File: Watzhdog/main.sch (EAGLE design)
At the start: 45 parts, among them IC1 C8051F381-GM, IC3 N25Q512A, IC6 MPU-9250, U1 MCP73831, U2 TPS61201

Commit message: Routed some airwires
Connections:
- removed net GND: C1.2, C12.2, C3.2, C4.2, C5.2, JP1.-, JP9.GND, R1.2, R4.2, R5.1, U1.VSS, U2.GND, U2.PAD@1, U2.PAD@2, U2.PAD@3, U2.PAD@4, U2.PAD@5, U2.PGND, U2.PS
- net DGND: now also C1.2, C12.2, C3.2, C4.2, C5.2, JP1.-, JP9.GND, R1.2, R4.2, R5.1, U1.VSS, U2.GND, U2.PAD@1, U2.PAD@2, U2.PAD@3, U2.PAD@4, U2.PAD@5, U2.PGND, U2.PS

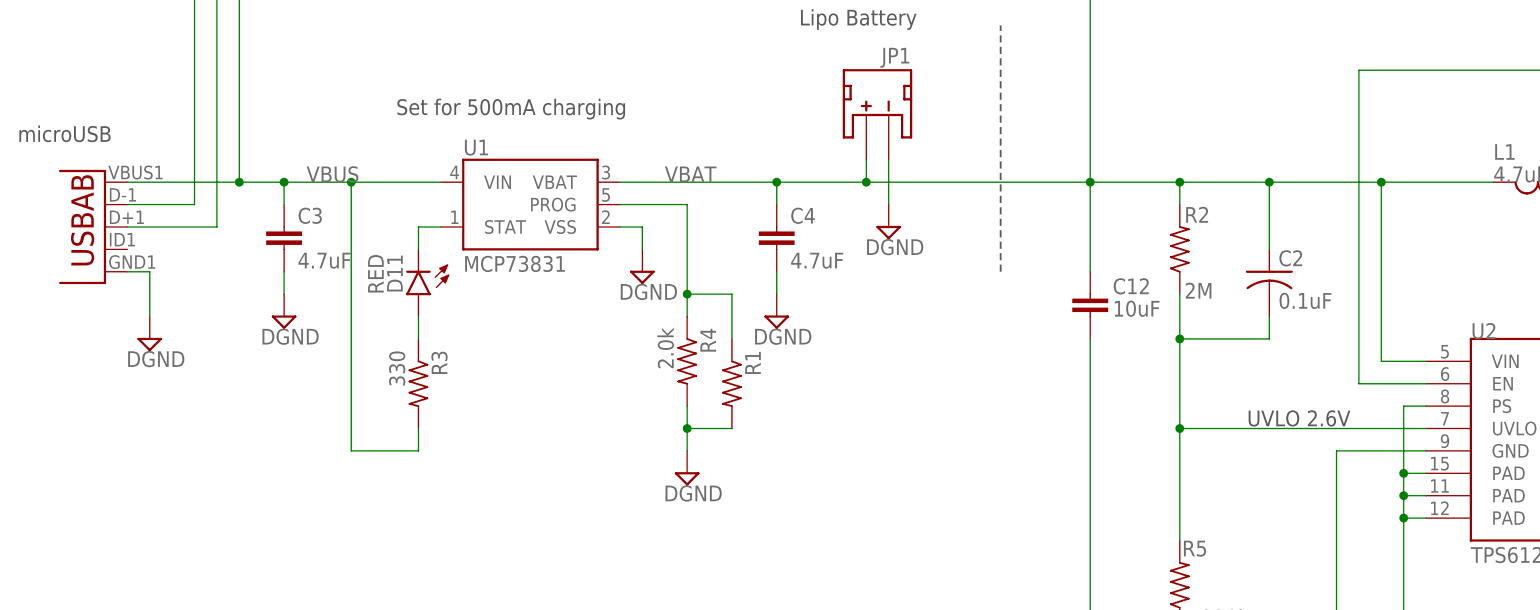
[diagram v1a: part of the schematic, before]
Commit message: Delete unnecessary resistances
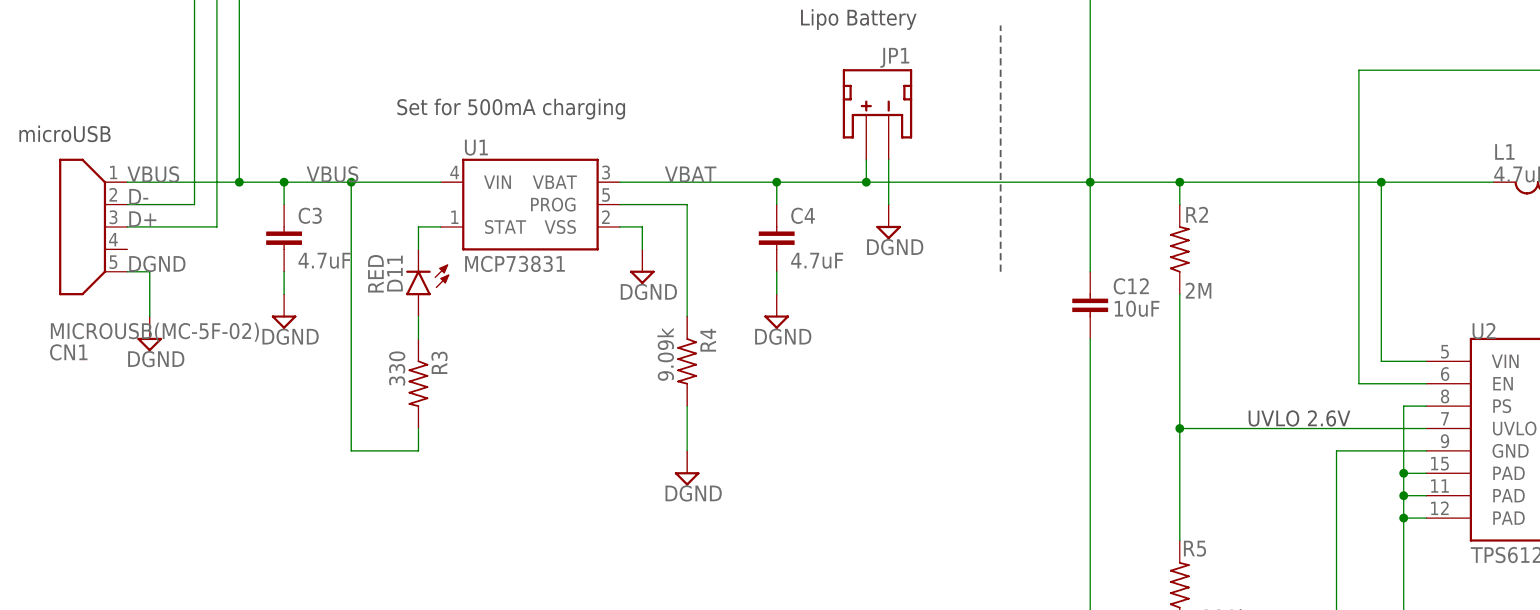
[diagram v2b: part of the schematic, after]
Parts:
- removed C2: 0.1uF, rcl:C-USC0402K
- removed JP9: Micro USB, SparkFun-Connectors:USB-ABCONN-11794
- removed R1: (no value), rcl:R-US_R0402
- added CN1: MICROUSB(MC-5F-02), Connector:MICROUSB(MC-5F-02)
- R4: value 2.0k -> 9.09k
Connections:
- net D+: now also CN1.P$3; no longer JP9.D+
- net D-: now also CN1.P$2; no longer JP9.D-
- net DGND: now also CN1.P$5; no longer JP9.GND, R1.2
- net PROG: no longer R1.1
- net UVLO: no longer C2.2
- net VBAT: no longer C2.1
- net VBUS: now also CN1.P$1; no longer JP9.VBUS
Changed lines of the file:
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@@
 <part name="GND18" library="supply2" library_urn="urn:adsk.eagle:library:372" deviceset="DGND" device=""/>
 <part name="U1" library="SparkFun-PowerIC" deviceset="MCP73831" device=""/>
-<part name="R4" library="rcl" library_urn="urn:adsk.eagle:library:334" deviceset="R-US_" device="R0402" package3d_urn="urn:adsk.eagle:package:23547/2" value="2.0k"/>
+<part name="R4" library="rcl" library_urn="urn:adsk.eagle:library:334" deviceset="R-US_" device="R0402" package3d_urn="urn:adsk.eagle:package:23547/2" value="9.09k"/>
 <part name="GND19" library="supply2" library_urn="urn:adsk.eagle:library:372" deviceset="DGND" device=""/>
 <part name="C3" library="SparkFun-Capacitors" deviceset="4.7UF-6.3V-10%(0603)" device="0603" value="4.7uF"/>
 <part name="C4" library="SparkFun-Capacitors" deviceset="4.7UF-6.3V-10%(0603)" device="0603" value="4.7uF"/>
-<part name="JP9" library="SparkFun-Connectors" deviceset="USB-AB" device="CONN-11794" value="Micro USB"/>
 <part name="JP1" library="SparkFun-Connectors" deviceset="JST_2MM_MALE" device="" value="JST"/>
 <part name="C1" library="CH_passive" deviceset="CAP" device="0805" value="22uF"/>
 <part name="U2" library="SparkFun" deviceset="TPS61200" device="" value="TPS61201"/>
-<part name="C2" library="rcl" library_urn="urn:adsk.eagle:library:334" deviceset="C-US" device="C0402K" package3d_urn="urn:adsk.eagle:package:23679/2" value="0.1uF"/>
 <part name="C5" library="rcl" library_urn="urn:adsk.eagle:library:334" deviceset="C-US" device="C0402K" package3d_urn="urn:adsk.eagle:package:23679/2" value="0.1uF"/>
 <part name="R2" library="rcl" library_urn="urn:adsk.eagle:library:334" deviceset="R-US_" device="R0402" package3d_urn="urn:adsk.eagle:package:23547/2" value="2M"/>
@@
 <part name="SUPPLY3" library="supply2" deviceset="DGND" device=""/>
 <part name="SUPPLY5" library="supply2" deviceset="DGND" device=""/>
-<part name="R1" library="rcl" library_urn="urn:adsk.eagle:library:334" deviceset="R-US_" device="R0402" package3d_urn="urn:adsk.eagle:package:23547/2"/>
 <part name="MN" library="testpad" deviceset="PTR1" device="TP10R"/>
 <part name="MP" library="testpad" deviceset="PTR1" device="TP10R"/>
@@
 <part name="JP3" library="pinhead" library_urn="urn:adsk.eagle:library:325" deviceset="PINHD-1X3" device="" package3d_urn="urn:adsk.eagle:package:22458/2"/>
 <part name="C12" library="CH_passive" deviceset="CAP" device="1206" value="10uF"/>
+<part name="CN1" library="Connector" deviceset="MICROUSB(MC-5F-02)" device=""/>
 </parts>
 <sheets>
@@
 <instance part="C3" gate="G$1" x="25.4" y="15.24"/>
 <instance part="C4" gate="G$1" x="81.28" y="15.24"/>
-<instance part="JP9" gate="G$1" x="2.54" y="17.78" smashed="yes" rot="R180"/>
 <instance part="JP1" gate="G$1" x="93.98" y="30.48" rot="MR0"/>
 <instance part="C1" gate="G$1" x="215.9" y="-7.62" smashed="yes">
@@
 </instance>
 <instance part="U2" gate="G$1" x="172.72" y="-5.08"/>
-<instance part="C2" gate="G$1" x="137.16" y="12.7"/>
 <instance part="C5" gate="G$1" x="198.12" y="-22.86"/>
 <instance part="R2" gate="G$1" x="127" y="15.24" smashed="yes" rot="R90">
@@
 <instance part="SUPPLY3" gate="G$1" x="375.92" y="-86.36"/>
 <instance part="SUPPLY5" gate="G$1" x="353.06" y="-86.36"/>
-<instance part="R1" gate="G$1" x="76.2" y="0" rot="R270"/>
 <instance part="MN" gate="G$1" x="350.52" y="-63.5" rot="R270"/>
 <instance part="MP" gate="G$1" x="350.52" y="-55.88" rot="R270"/>
@@
 <attribute name="VALUE" x="119.38" y="7.62" size="1.778" layer="96"/>
 </instance>
+<instance part="CN1" gate="G$1" x="0" y="17.78"/>
 </instances>
 <busses>
@@
 <segment>
 <wire x1="127" y1="20.32" x2="127" y2="22.86" width="0.1524" layer="91"/>
-<wire x1="127" y1="22.86" x2="137.16" y2="22.86" width="0.1524" layer="91"/>
-<wire x1="137.16" y1="22.86" x2="149.86" y2="22.86" width="0.1524" layer="91"/>
+<wire x1="127" y1="22.86" x2="149.86" y2="22.86" width="0.1524" layer="91"/>
 <wire x1="116.84" y1="12.7" x2="116.84" y2="22.86" width="0.1524" layer="91"/>
 <wire x1="116.84" y1="22.86" x2="127" y2="22.86" width="0.1524" layer="91"/>
 <wire x1="162.56" y1="22.86" x2="149.86" y2="22.86" width="0.1524" layer="91"/>
-<wire x1="137.16" y1="15.24" x2="137.16" y2="22.86" width="0.1524" layer="91"/>
 <wire x1="154.94" y1="2.54" x2="149.86" y2="2.54" width="0.1524" layer="91"/>
 <wire x1="149.86" y1="22.86" x2="149.86" y2="2.54" width="0.1524" layer="91"/>
@@
 <junction x="116.84" y="22.86"/>
 <junction x="149.86" y="22.86"/>
-<junction x="137.16" y="22.86"/>
 <pinref part="U2" gate="G$1" pin="VIN"/>
-<pinref part="C2" gate="G$1" pin="1"/>
 <pinref part="R2" gate="G$1" pin="2"/>
 <pinref part="L1" gate="G$1" pin="2"/>
@@
 <segment>
 <wire x1="63.5" y1="20.32" x2="71.12" y2="20.32" width="0.1524" layer="91"/>
-<wire x1="71.12" y1="20.32" x2="71.12" y2="10.16" width="0.1524" layer="91"/>
+<wire x1="71.12" y1="20.32" x2="71.12" y2="7.62" width="0.1524" layer="91"/>
 <pinref part="U1" gate="G$1" pin="PROG"/>
 <pinref part="R4" gate="G$1" pin="1"/>
-<wire x1="71.12" y1="10.16" x2="71.12" y2="7.62" width="0.1524" layer="91"/>
-<wire x1="76.2" y1="5.08" x2="76.2" y2="10.16" width="0.1524" layer="91"/>
-<wire x1="76.2" y1="10.16" x2="71.12" y2="10.16" width="0.1524" layer="91"/>
-<junction x="71.12" y="10.16"/>
-<pinref part="R1" gate="G$1" pin="1"/>
 </segment>
 </net>
@@
 <net name="UVLO" class="0">
 <segment>
-<wire x1="127" y1="10.16" x2="127" y2="5.08" width="0.1524" layer="91"/>
-<wire x1="127" y1="5.08" x2="127" y2="-5.08" width="0.1524" layer="91"/>
+<wire x1="127" y1="10.16" x2="127" y2="-5.08" width="0.1524" layer="91"/>
 <wire x1="127" y1="-5.08" x2="127" y2="-17.78" width="0.1524" layer="91"/>
 <wire x1="154.94" y1="-5.08" x2="127" y2="-5.08" width="0.1524" layer="91"/>
-<wire x1="137.16" y1="7.62" x2="137.16" y2="5.08" width="0.1524" layer="91"/>
-<wire x1="137.16" y1="5.08" x2="127" y2="5.08" width="0.1524" layer="91"/>
 <junction x="127" y="-5.08"/>
-<junction x="127" y="5.08"/>
 <pinref part="U2" gate="G$1" pin="UVLO"/>
-<pinref part="C2" gate="G$1" pin="2"/>
 <pinref part="R2" gate="G$1" pin="1"/>
 <pinref part="R5" gate="G$1" pin="2"/>
@@
 </segment>
 <segment>
-<wire x1="71.12" y1="-7.62" x2="71.12" y2="-5.08" width="0.1524" layer="91"/>
 <pinref part="R4" gate="G$1" pin="2"/>
 <pinref part="GND19" gate="G$1" pin="DGND"/>
-<wire x1="71.12" y1="-5.08" x2="71.12" y2="-2.54" width="0.1524" layer="91"/>
-<wire x1="76.2" y1="-5.08" x2="71.12" y2="-5.08" width="0.1524" layer="91"/>
-<junction x="71.12" y="-5.08"/>
-<pinref part="R1" gate="G$1" pin="2"/>
+<wire x1="71.12" y1="-7.62" x2="71.12" y2="-2.54" width="0.1524" layer="91"/>
 </segment>
 <segment>
 <pinref part="GND15" gate="G$1" pin="DGND"/>
-<pinref part="JP9" gate="G$1" pin="GND"/>
 <wire x1="10.16" y1="7.62" x2="10.16" y2="12.7" width="0.1524" layer="91"/>
 <wire x1="10.16" y1="12.7" x2="7.62" y2="12.7" width="0.1524" layer="91"/>
+<pinref part="CN1" gate="G$1" pin="P$5"/>
+<label x="7.62" y="12.7" size="1.778" layer="95"/>
 </segment>
 <segment>
@@
 <pinref part="U1" gate="G$1" pin="VIN"/>
 <pinref part="C3" gate="G$1" pin="1"/>
-<pinref part="JP9" gate="G$1" pin="VBUS"/>
 <wire x1="20.32" y1="22.86" x2="25.4" y2="22.86" width="0.1524" layer="91"/>
 <wire x1="20.32" y1="48.26" x2="20.32" y2="22.86" width="0.1524" layer="91"/>
 <junction x="20.32" y="22.86"/>
+<pinref part="CN1" gate="G$1" pin="P$1"/>
+<label x="7.62" y="22.86" size="1.778" layer="95"/>
 </segment>
 </net>
@@
 <wire x1="292.1" y1="55.88" x2="15.24" y2="55.88" width="0.1524" layer="91"/>
 <wire x1="15.24" y1="55.88" x2="15.24" y2="20.32" width="0.1524" layer="91"/>
-<pinref part="JP9" gate="G$1" pin="D-"/>
 <wire x1="15.24" y1="20.32" x2="7.62" y2="20.32" width="0.1524" layer="91"/>
+<pinref part="CN1" gate="G$1" pin="P$2"/>
+<label x="7.62" y="20.32" size="1.778" layer="95"/>
 </segment>
 </net>
@@
 <wire x1="297.18" y1="58.42" x2="17.78" y2="58.42" width="0.1524" layer="91"/>
 <wire x1="17.78" y1="58.42" x2="17.78" y2="17.78" width="0.1524" layer="91"/>
-<pinref part="JP9" gate="G$1" pin="D+"/>
 <wire x1="17.78" y1="17.78" x2="7.62" y2="17.78" width="0.1524" layer="91"/>
-</segment>
-</net>
+<pinref part="CN1" gate="G$1" pin="P$3"/>
+<label x="7.62" y="17.78" size="1.778" layer="95"/>
+</segment>
+</net>
